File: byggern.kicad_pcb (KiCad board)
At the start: 2 copper layers, 41 parts, among them J1 Power_Rail, J2 JTAG LINK, J3 OLED_Connection, J4 CAN, J5 P1000 Header, J6 DB9_Female_MountingHoles, U1 Barrel_jack, U10 MAX233, U2 LM340SX, U3 ATmega162-16PU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

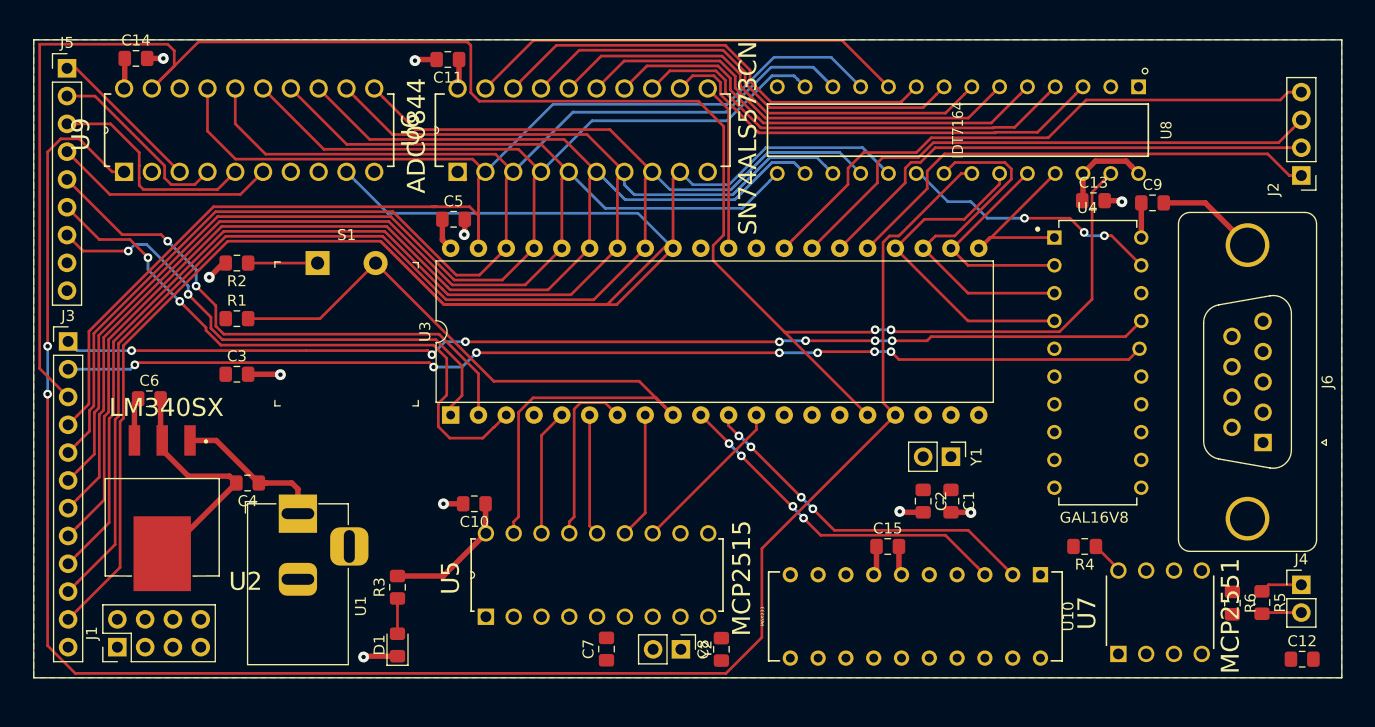
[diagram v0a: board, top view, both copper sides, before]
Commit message: Change footprints of ICs to DIPs and Close to finish routing
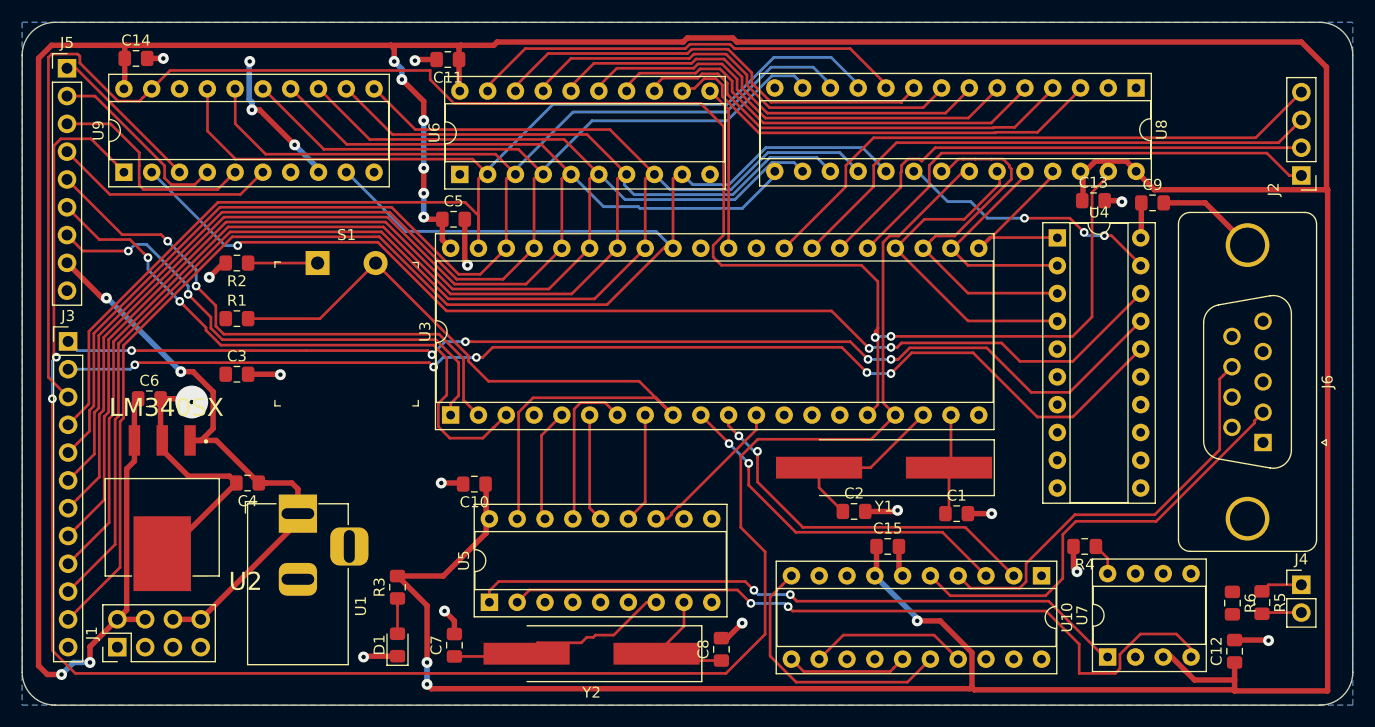
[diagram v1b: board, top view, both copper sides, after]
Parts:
- C11: value C_Small -> 0.1uF
- U10: footprint byggern:MAX233CPP -> Package_DIP:DIP-20_W7.62mm_Socket
- U3: footprint Package_DIP:DIP-40_W15.24mm -> Package_DIP:DIP-40_W15.24mm_Socket
- U4: footprint byggern:GAL16V8 -> Package_DIP:DIP-20_W7.62mm_Socket
- U5: footprint byggern:MCP2515-EP -> Package_DIP:DIP-18_W7.62mm_Socket
- U6: footprint byggern:SN74ALS573CN -> Package_DIP:DIP-20_W7.62mm_Socket
- U7: footprint byggern:MCP2551-IP -> Package_DIP:DIP-8_W7.62mm_Socket
- U8: footprint byggern:CY7C185-20PC -> Package_DIP:DIP-28_W7.62mm_Socket
- U9: footprint byggern:ADC0844CCN -> Package_DIP:DIP-20_W7.62mm_Socket
- Y1, Y2: footprint Connector_PinHeader_2.54mm:PinHeader_1x02_P2.54mm_Vertical -> Crystal:Crystal_SMD_HC49-SD_HandSoldering
- moved U10 24.2 mm to (181.0, 125.2)
- moved U9 24.1 mm to (97.1, 88.3)
- moved U6 24.0 mm to (127.8, 88.5)
- moved U5 21.0 mm to (130.5, 127.6)
- moved U8 16.7 mm to (189.6, 80.6)
- moved C7 13.9 mm to (127.3, 131.5)
- moved U4 12.0 mm to (182.4, 94.3)
- moved U7 11.7 mm to (187.0, 132.6)
- moved Y2 8.17 mm to (139.9, 132.3), turned to 180 degrees
- moved C2 6.39 mm to (163.9, 119.3), turned to 0 degrees
- moved C12 6.22 mm to (198.6, 132.1), turned to 90 degrees
- moved Y1 6.20 mm to (166.6, 115.3), turned to 180 degrees
- moved C10 1.80 mm to (129.2, 116.8)
- moved C1 1.26 mm to (173.2, 119.5), turned to 0 degrees
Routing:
- net VCC: track 39.2 -> 474.5 mm, vias 0 -> 14
- net /~CS~_ADC: track 0.00 -> 100.8 mm, vias 0 -> 3
- net Net-(U5-Pad2): track 0.00 -> 70.1 mm, vias 0 -> 2
- net Net-(U5-Pad1): track 0.00 -> 61.0 mm, vias 0 -> 2
- net Net-(J6-Pad2): track 0.00 -> 40.6 mm
- net +12V: track 13.9 -> 54.0 mm, vias 0 -> 2
- net Net-(J6-Pad8): track 0.00 -> 38.6 mm
- net /A7: track 178.3 -> 147.4 mm
- net Net-(U10-Pad10): track 0.00 -> 24.7 mm
- net Net-(C7-Pad1): track 0.00 -> 20.5 mm
- net GND: track 55.5 -> 73.0 mm, vias 10 -> 15
- net Net-(C2-Pad1): track 0.00 -> 16.4 mm
- net Net-(U10-Pad12): track 0.00 -> 14.5 mm
- net Net-(C8-Pad1): track 0.00 -> 11.9 mm
- net Net-(U10-Pad11): track 0.00 -> 11.1 mm
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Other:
- board outline added: 121.6 x 62.4 mm

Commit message: Fix errors and update BOM
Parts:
- removed R6: 120, Resistor_SMD:R_0805_2012Metric_Pad1.15x1.40mm_HandSolder
- added TP1: TestPoint, TestPoint:TestPoint_Pad_D1.5mm, F.Cu at (149.8, 92.0)
- added TP10: TestPoint, TestPoint:TestPoint_Pad_D1.5mm, F.Cu at (154.2, 92.0)
- added TP11: TestPoint, TestPoint:TestPoint_Pad_D1.5mm, F.Cu at (194.0, 81.4)
- added TP12: TestPoint, TestPoint:TestPoint_Pad_D1.5mm, F.Cu at (99.6, 92.0)
- added TP2: TestPoint, TestPoint:TestPoint_Pad_D1.5mm, F.Cu at (108.2, 110.4)
- added TP3: TestPoint, TestPoint:TestPoint_Pad_D1.5mm, F.Cu at (136.8, 115.4)
- added TP4: TestPoint, TestPoint:TestPoint_Pad_D1.5mm, F.Cu at (141.2, 117.0)
- added TP5: TestPoint, TestPoint:TestPoint_Pad_D1.5mm, F.Cu at (146.8, 114.2)
- added TP6: TestPoint, TestPoint:TestPoint_Pad_D1.5mm, F.Cu at (150.2, 114.2)
- added TP7: TestPoint, TestPoint:TestPoint_Pad_D1.5mm, F.Cu at (141.2, 113.8)
- added TP8: TestPoint, TestPoint:TestPoint_Pad_D1.5mm, F.Cu at (150.2, 117.0)
- added TP9: TestPoint, TestPoint:TestPoint_Pad_D1.5mm, F.Cu at (146.8, 117.0)
- J2: footprint Connector_PinHeader_2.54mm:PinHeader_1x04_P2.54mm_Vertical -> Connector_PinHeader_2.54mm:PinHeader_2x04_P2.54mm_Vertical
- J6: value DB9_Female_MountingHoles -> A-DF_09_A_KG-T2S; footprint Connector_Dsub:DSUB-9_Female_Vertical_P2.77x2.84mm_MountingHoles -> digikey-footprints:DSUB-9_Receptical_A-DF_09_A_KG-T2S
- moved J6 9.60 mm to (193.2, 107.7)
- moved U4 2.40 mm to (180.0, 94.3)
- moved J2 0.41 mm to (204.8, 88.2)
- moved C9 0.41 mm to (191.4, 90.8)
- moved U7 0.22 mm to (187.0, 132.8)
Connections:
- net Net-(J6-Pad2) renamed /TO2
- J2 pad 2: Net-(J2-Pad2) -> VCC
- J2 pad 4: Net-(J2-Pad4) -> (no net)
- J6 pad 1: Net-(J6-Pad1) -> (no net)
- J6 pad 3: Net-(J6-Pad3) -> /TO3
- J6 pad 4: Net-(J6-Pad4) -> (no net)
- J6 pad 6: Net-(J6-Pad6) -> (no net)
- J6 pad 7: Net-(J6-Pad7) -> (no net)
- J6 pad 8: Net-(J6-Pad8) -> (no net)
- J6 pad 9: Net-(J6-Pad9) -> (no net)
- U10 pad 1: Net-(U10-Pad1) -> (no net)
- U10 pad 13: Net-(U10-Pad13) -> (no net)
- U10 pad 14: Net-(U10-Pad14) -> (no net)
- U10 pad 18: Net-(U10-Pad18) -> (no net)
- U10 pad 19: Net-(U10-Pad19) -> (no net)
- U10 pad 20: Net-(U10-Pad20) -> (no net)
- U10 pad 4: Net-(J6-Pad8) -> /TO3
- U10 pad 8: Net-(U10-Pad8) -> (no net)
- U3 pad 13: Net-(U3-Pad13) -> (no net)
- U3 pad 14: Net-(U3-Pad14) -> (no net)
- U3 pad 15: Net-(U3-Pad15) -> (no net)
- U3 pad 26: Net-(J2-Pad2) -> Net-(J2-Pad3)
- U3 pad 27: Net-(J2-Pad3) -> Net-(J2-Pad5)
- U3 pad 28: Net-(J2-Pad4) -> Net-(J2-Pad7)
- U3 pad 29: Net-(U3-Pad29) -> (no net)
- U3 pad 31: Net-(U3-Pad31) -> /ADC_~INT~
- U3 pad 4: Net-(U3-Pad4) -> (no net)
- U4 pad 1: /A8 -> /A11
- U4 pad 11: Net-(U4-Pad11) -> (no net)
- U4 pad 12: Net-(U4-Pad12) -> (no net)
- U4 pad 13: Net-(U4-Pad13) -> (no net)
- U4 pad 14: Net-(U4-Pad14) -> (no net)
- U4 pad 15: Net-(U4-Pad15) -> (no net)
- U4 pad 19: /~CS~_RAM -> /CS_RAM
- U4 pad 2: /A9 -> /A10
- U4 pad 3: /A10 -> /A9
- U4 pad 4: /A11 -> /A8
- U4 pad 5: Net-(U4-Pad5) -> (no net)
- U4 pad 6: Net-(U4-Pad6) -> (no net)
- U4 pad 7: Net-(U4-Pad7) -> (no net)
- U4 pad 8: Net-(U4-Pad8) -> (no net)
- U4 pad 9: Net-(U4-Pad9) -> (no net)
- U5 pad 10: Net-(U5-Pad10) -> (no net)
- U5 pad 11: Net-(U5-Pad11) -> (no net)
- U5 pad 3: Net-(U5-Pad3) -> (no net)
- U5 pad 4: Net-(U5-Pad4) -> (no net)
- U5 pad 5: Net-(U5-Pad5) -> (no net)
- U5 pad 6: Net-(U5-Pad6) -> (no net)
- U7 pad 5: Net-(U7-Pad5) -> (no net)
- U8 pad 1: Net-(U8-Pad1) -> (no net)
- U8 pad 20: /~CS~_RAM -> GND
- U8 pad 26: VCC -> /CS_RAM
- U9 pad 18: Net-(U9-Pad18) -> /ADC_~INT~
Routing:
- net /ADC_~INT~: track 0.00 -> 68.4 mm, vias 0 -> 4
- net Net-(J2-Pad7): track 0.00 -> 56.7 mm
- net Net-(J2-Pad5): track 0.00 -> 55.7 mm
- net Net-(J2-Pad4): track 54.3 -> 0.00 mm
- net Net-(J2-Pad2): track 47.3 -> 0.00 mm
- net Net-(J6-Pad8): track 38.6 -> 0.00 mm
- net /TO3: track 0.00 -> 33.0 mm
- net Net-(J4-Pad1): track 3.85 -> 34.8 mm
- net /CS_RAM: track 0.00 -> 26.4 mm, vias 0 -> 2
- net VCC: track 474.5 -> 499.7 mm, vias 14 -> 16
- net /~CS~_RAM: track 24.0 -> 0.00 mm, vias 3 -> 0
- net /~OE~: track 181.9 -> 200.9 mm
- net /~WR~: track 175.9 -> 194.1 mm, vias 2 -> 4
- net /CAN_~INT~: track 13.9 -> 27.3 mm, vias 0 -> 1
- net /~RESET~: track 72.1 -> 85.2 mm, vias 0 -> 2
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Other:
- board text added: "+12V"
- board text added: "ADC0844"
- board text added: "ATmega162"
- board text added: "BYGGERN NODE 1"
- board text added: "B_L"
- board text added: "B_R"
- board text added: "CAN"
- board text added: "CH1"
- board text added: "CH2"
- board text added: "CH3"
- board text added: "CH4"
- board text added: "GAL16V8"
- board text added: "GND"
- board text added: "IDT7164"
- board text added: "JTAG LINK"
- board text added: "MAX233"
- board text added: "MCP2515"
- board text added: "MCP2551"
- board text added: "OLED HEADER"
- board text added: "P1000 Header"
- board text added: "Rev 1.0 Designed by Sander Furre"
- board text added: "SN74ALS573CN"
- board text added: "SOUND_PWM"
- board text added: "StartOver"
